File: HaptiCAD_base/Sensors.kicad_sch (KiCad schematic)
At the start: 6 parts, among them U501 AP2112K-3.3

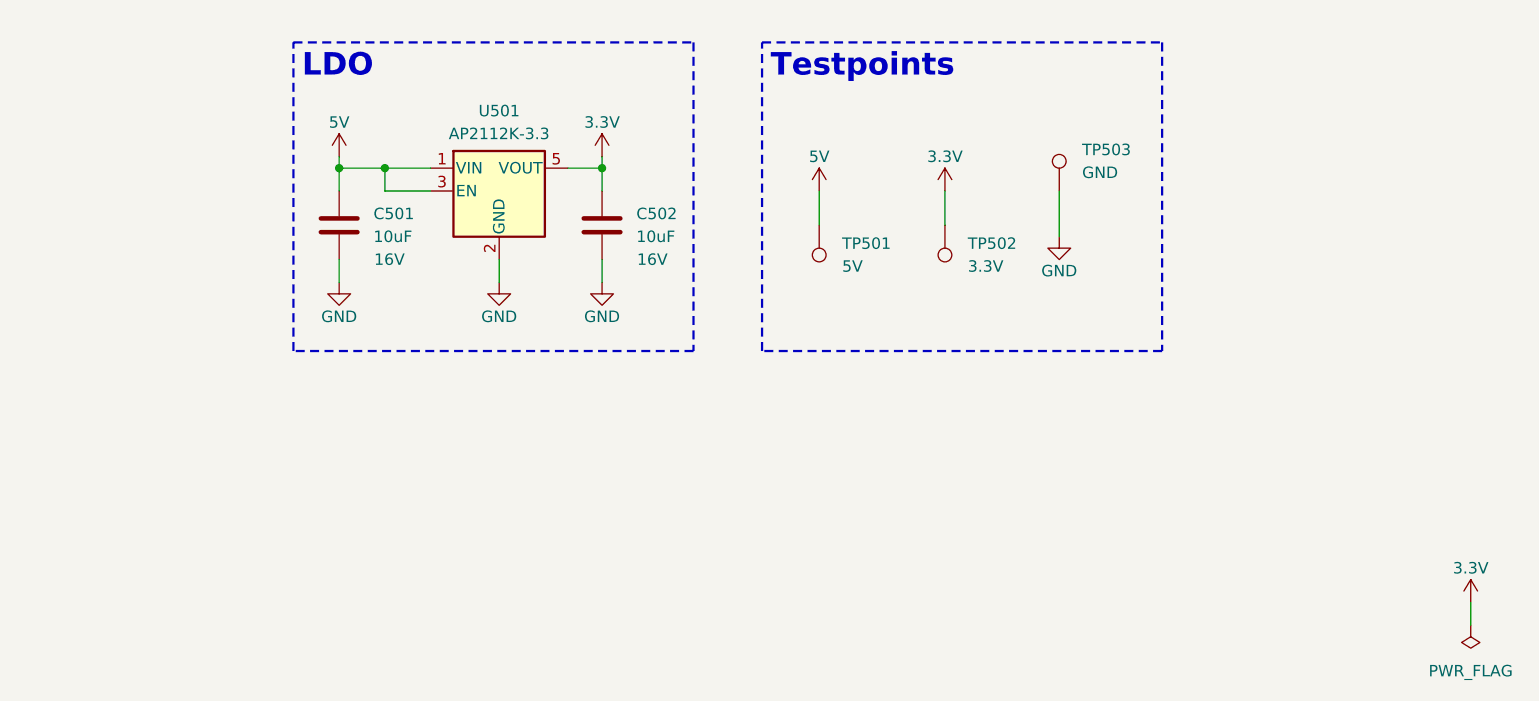
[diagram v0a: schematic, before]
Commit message: Split project into base and motor mount pcb
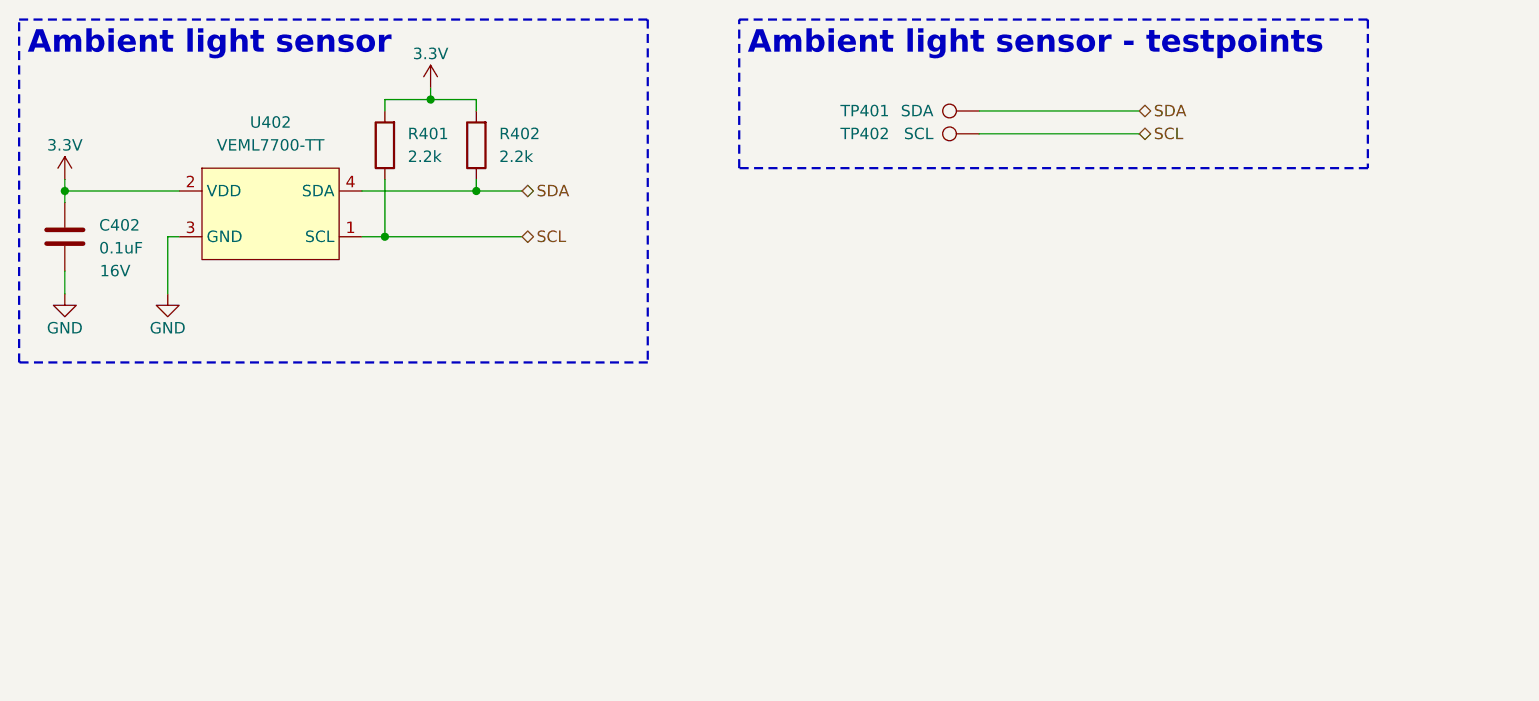
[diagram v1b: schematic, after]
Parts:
- removed C501, C502: 10uF, Capacitor_SMD:C_0805_2012Metric, symbol Device:C
- removed TP501: 5V, TestPoint:TestPoint_Pad_D1.0mm, symbol Connector:TestPoint
- removed TP502: 3.3V, TestPoint:TestPoint_Pad_D1.0mm, symbol Connector:TestPoint
- removed TP503: GND, TestPoint:TestPoint_Pad_D1.0mm, symbol Connector:TestPoint
- removed U501: AP2112K-3.3, Package_TO_SOT_SMD:SOT-23-5, symbol Regulator_Linear:AP2112K-3.3
- added C402: 0.1uF, Capacitor_SMD:C_0603_1608Metric, symbol Device:C
- added R401, R402: 2.2k, Resistor_SMD:R_0603_1608Metric, symbol Device:R
- added TP401: SDA, TestPoint:TestPoint_Pad_D1.0mm, symbol Connector:TestPoint
- added TP402: SCL, TestPoint:TestPoint_Pad_D1.0mm, symbol Connector:TestPoint
- added U402: VEML7700-TT, PCM_SparkFun-Sensor:VEML7700-TT, symbol PCM_SparkFun-Sensor:VEML7700-TT
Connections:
- net 3.3V: now also C402.1, R401.2, R402.2, U402.2 (VDD)
- net GND: now also C402.2, U402.3 (GND)
- new net SCL: R401.1, TP402.1, U402.1 (SCL)
- new net SDA: R402.1, TP401.1, U402.4 (SDA)
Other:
- title: Power -> Sensors

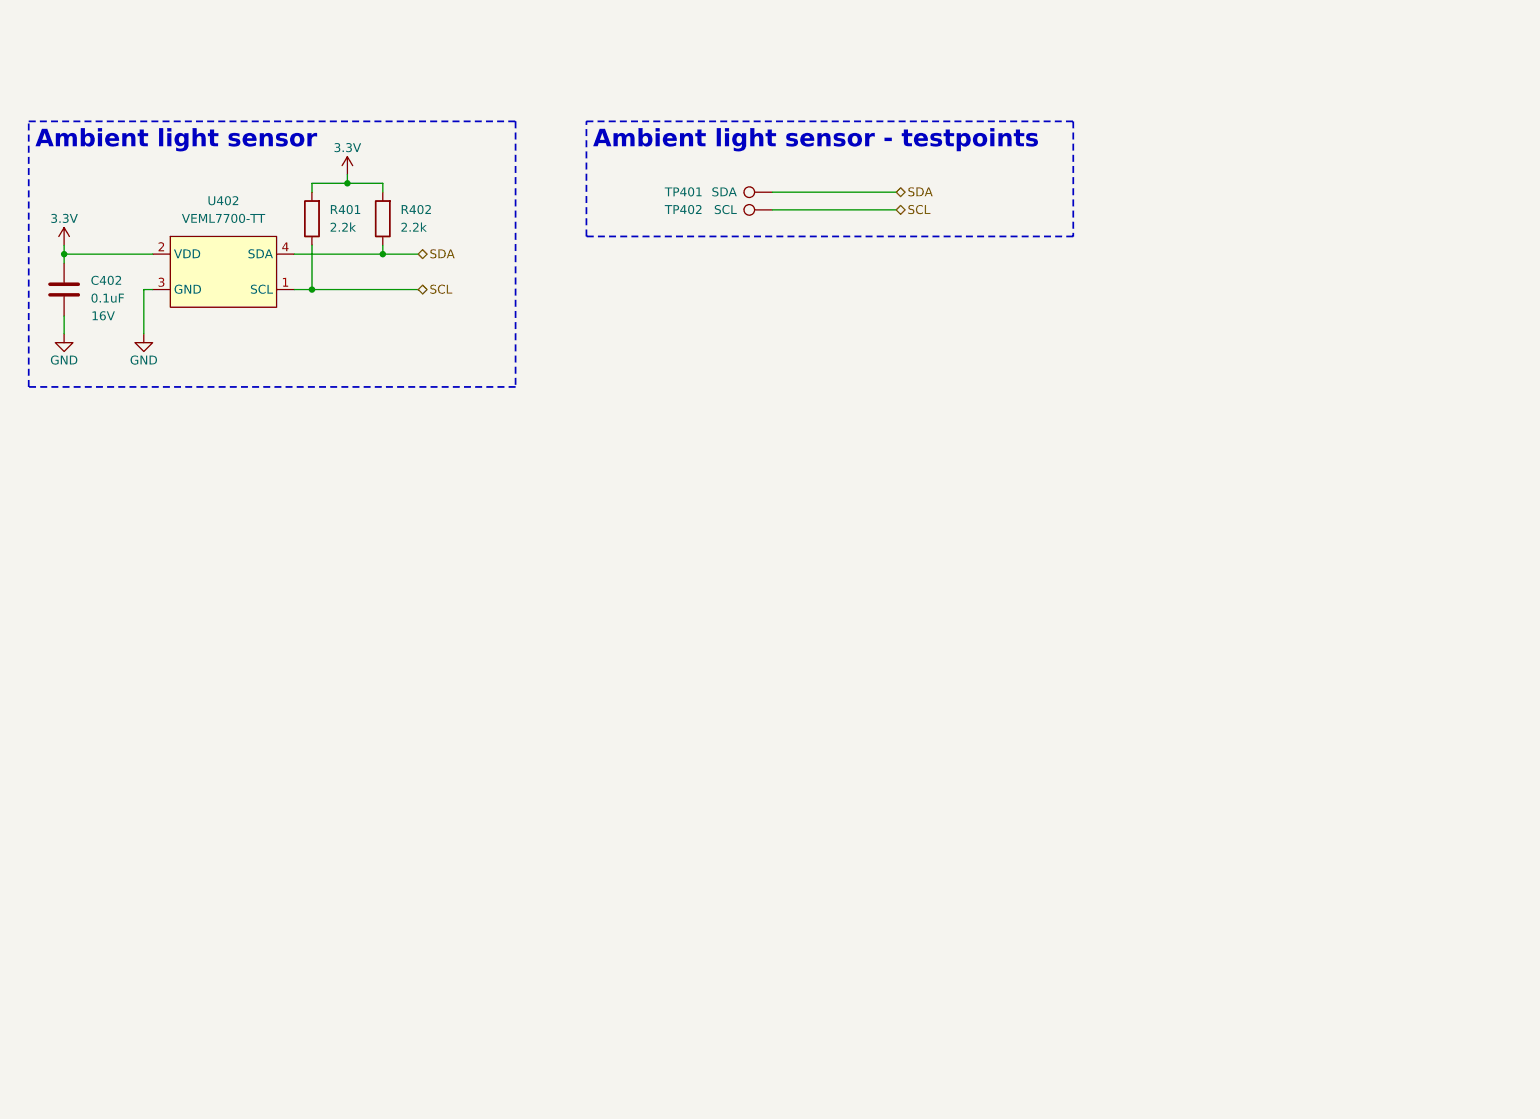
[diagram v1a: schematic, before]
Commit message: updated base schematic and PCB
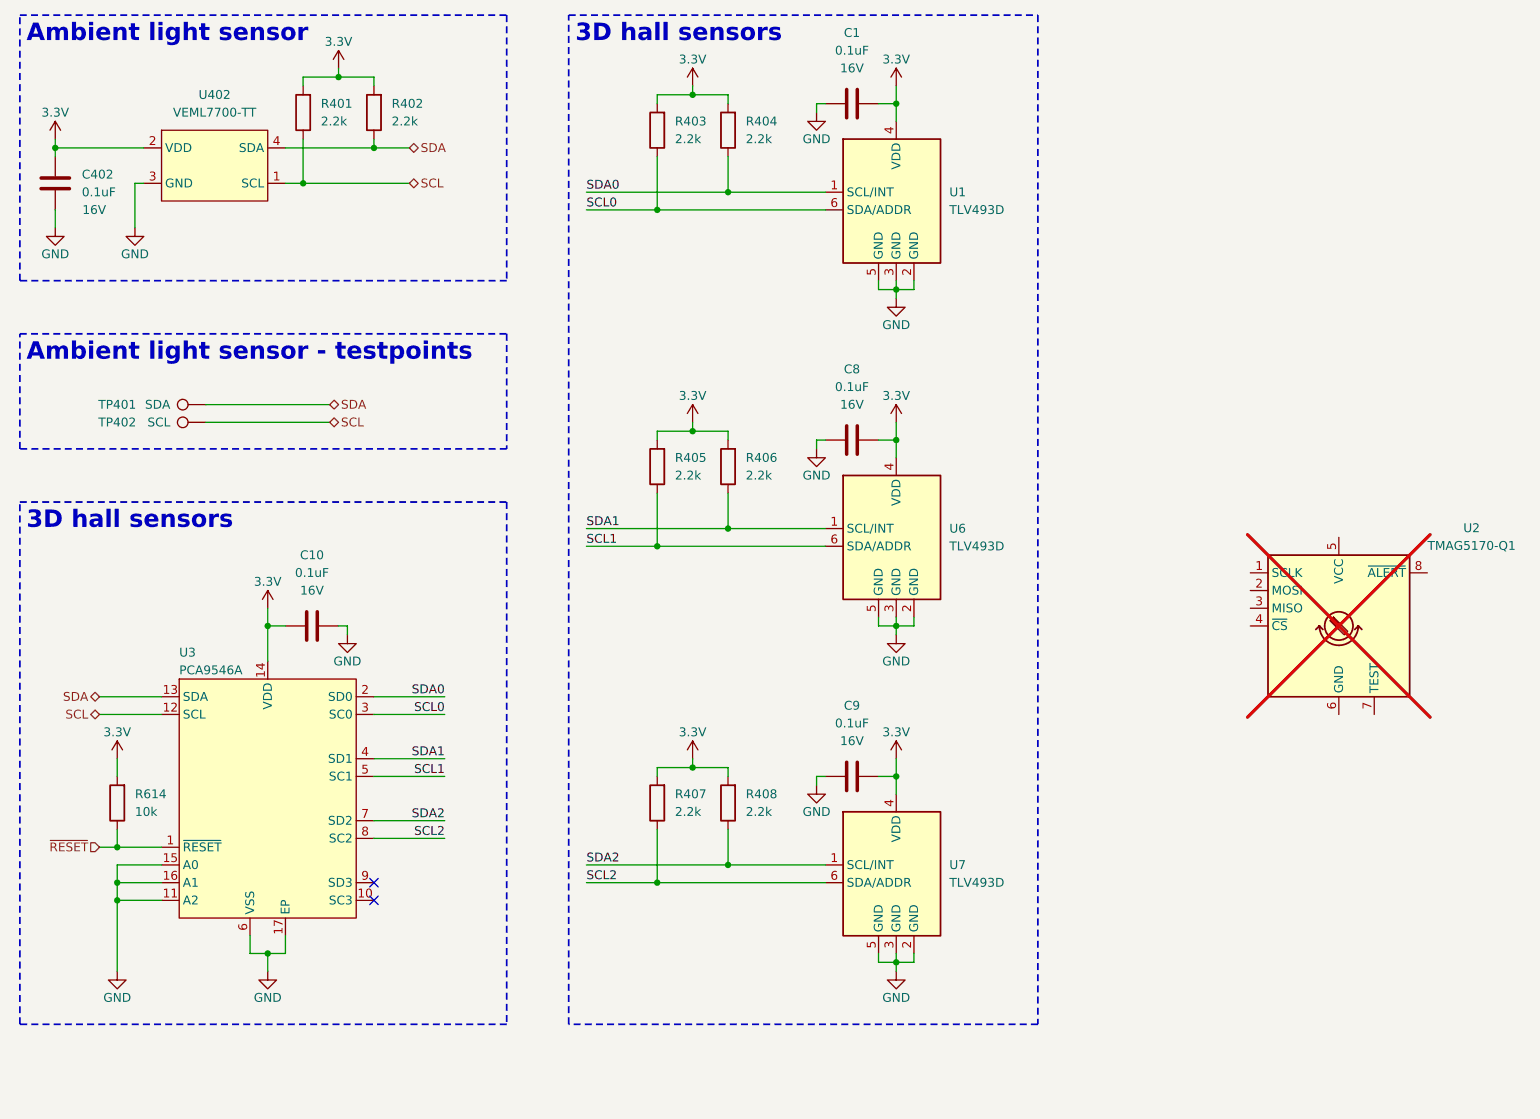
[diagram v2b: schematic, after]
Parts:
- added C1, C10, C8, C9: 0.1uF, Capacitor_SMD:C_0603_1608Metric, symbol Device:C
- added R403, R404, R405, R406, R407, R408: 2.2k, Resistor_SMD:R_0603_1608Metric, symbol Device:R
- added R614: 10k, Resistor_SMD:R_0402_1005Metric, symbol Device:R
- added U1, U6, U7: TLV493D, Package_TO_SOT_SMD:SOT-23-6, symbol Sensor_Magnetic:TLV493D
- added U2: TMAG5170-Q1, Package_SO:VSSOP-8_3x3mm_P0.65mm, symbol Sensor_Magnetic:TMAG5170-Q1
- added U3: PCA9546A, PCA9546A:QFN-16_EP_5.25x5.25_Pitch0.65mm, symbol PCA9546A:PCA9546A
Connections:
- net 3.3V: now also C1.2, C10.2, C8.2, C9.2, R403.2, R404.2, R405.2, R406.2, R407.2, R408.2, R614.2, U1.4 (VDD), U3.14 (VDD), U6.4 (VDD), U7.4 (VDD)
- net GND: now also C1.1, C10.1, C8.1, C9.1, U1.2 (GND), U1.3 (GND), U1.5 (GND), U3.11 (A2), U3.15 (A0), U3.16 (A1), U3.17 (EP), U3.6 (VSS), U6.2 (GND), U6.3 (GND), U6.5 (GND), U7.2 (GND), U7.3 (GND), U7.5 (GND)
- net SCL: now also U3.12 (SCL)
- net SDA: now also U3.13 (SDA)
- new net SCL0: R403.1, U1.6 (SDA/ADDR), U3.3 (SC0)
- new net SCL1: R405.1, U3.5 (SC1), U6.6 (SDA/ADDR)
- new net SCL2: R407.1, U3.8 (SC2), U7.6 (SDA/ADDR)
- new net SDA0: R404.1, U1.1 (SCL/INT), U3.2 (SD0)
- new net SDA1: R406.1, U3.4 (SD1), U6.1 (SCL/INT)
- new net SDA2: R408.1, U3.7 (SD2), U7.1 (SCL/INT)
- new net ~{RESET}: R614.1, U3.1 (~{RESET})
- no-connect marks 0 -> 2
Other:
- moved on the sheet: C402, R401, R402, TP401, TP402, U402

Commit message: Finished schematic of the base board
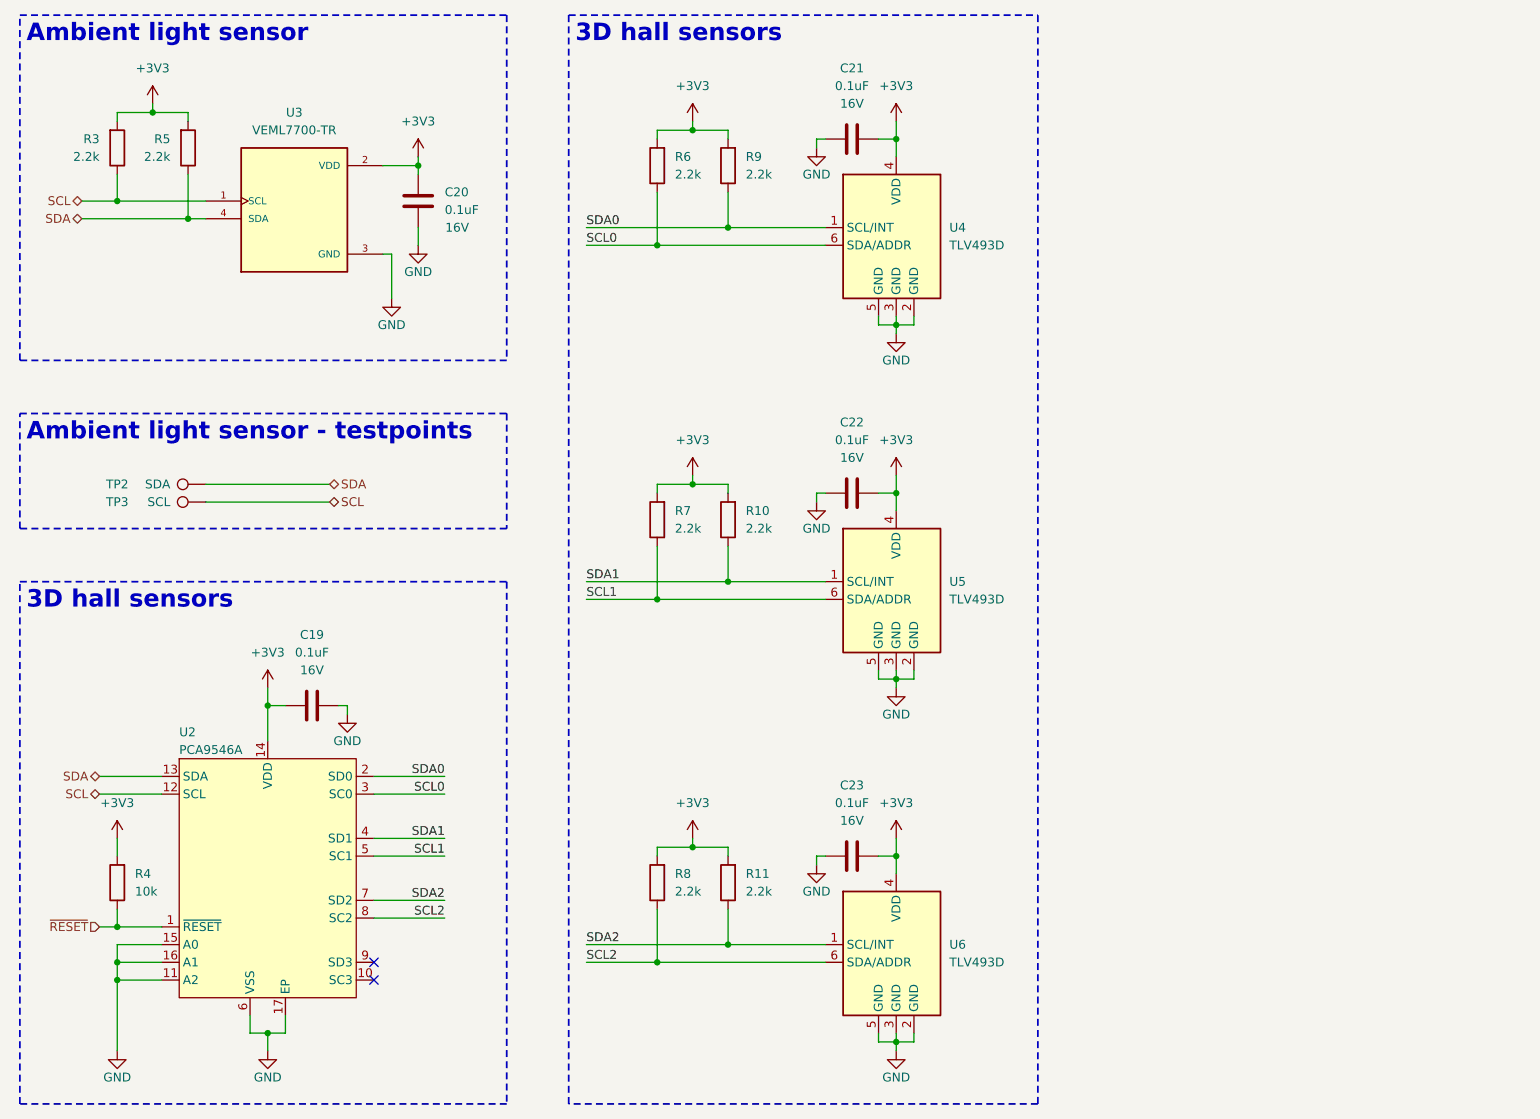
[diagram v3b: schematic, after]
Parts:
- removed U2: TMAG5170-Q1, Package_SO:VSSOP-8_3x3mm_P0.65mm, symbol Sensor_Magnetic:TMAG5170-Q1
- removed U402: VEML7700-TT, PCM_SparkFun-Sensor:VEML7700-TT, symbol PCM_SparkFun-Sensor:VEML7700-TT
- added U3: VEML7700-TR, VEML7700-TR:XDCR_VEML7700-TR, symbol VEML7700-TR:VEML7700-TR
- renumbered C10 to C19, C402 to C20, C1 to C21, C8 to C22, C9 to C23, R406 to R10, R408 to R11, R402 to R3, R614 to R4, R401 to R5, R403 to R6, R405 to R7, R407 to R8, R404 to R9, TP401 to TP2, TP402 to TP3, U3 to U2, U1 to U4, U6 to U5, U7 to U6
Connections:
- net GND: now also U3.3 (GND)
- net SCL: now also R3.1, U3.1 (SCL); no longer R5.1
- net SDA: now also R5.1, U3.4 (SDA); no longer R3.1
- net 3.3V renamed +3V3
- net +3V3: now also U3.2 (VDD)
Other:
- moved on the sheet: C19, C20, C21, C22, C23, R10, R11, R3, R4, R5, R6, R7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

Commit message: Finished the layout for the base and motor mount
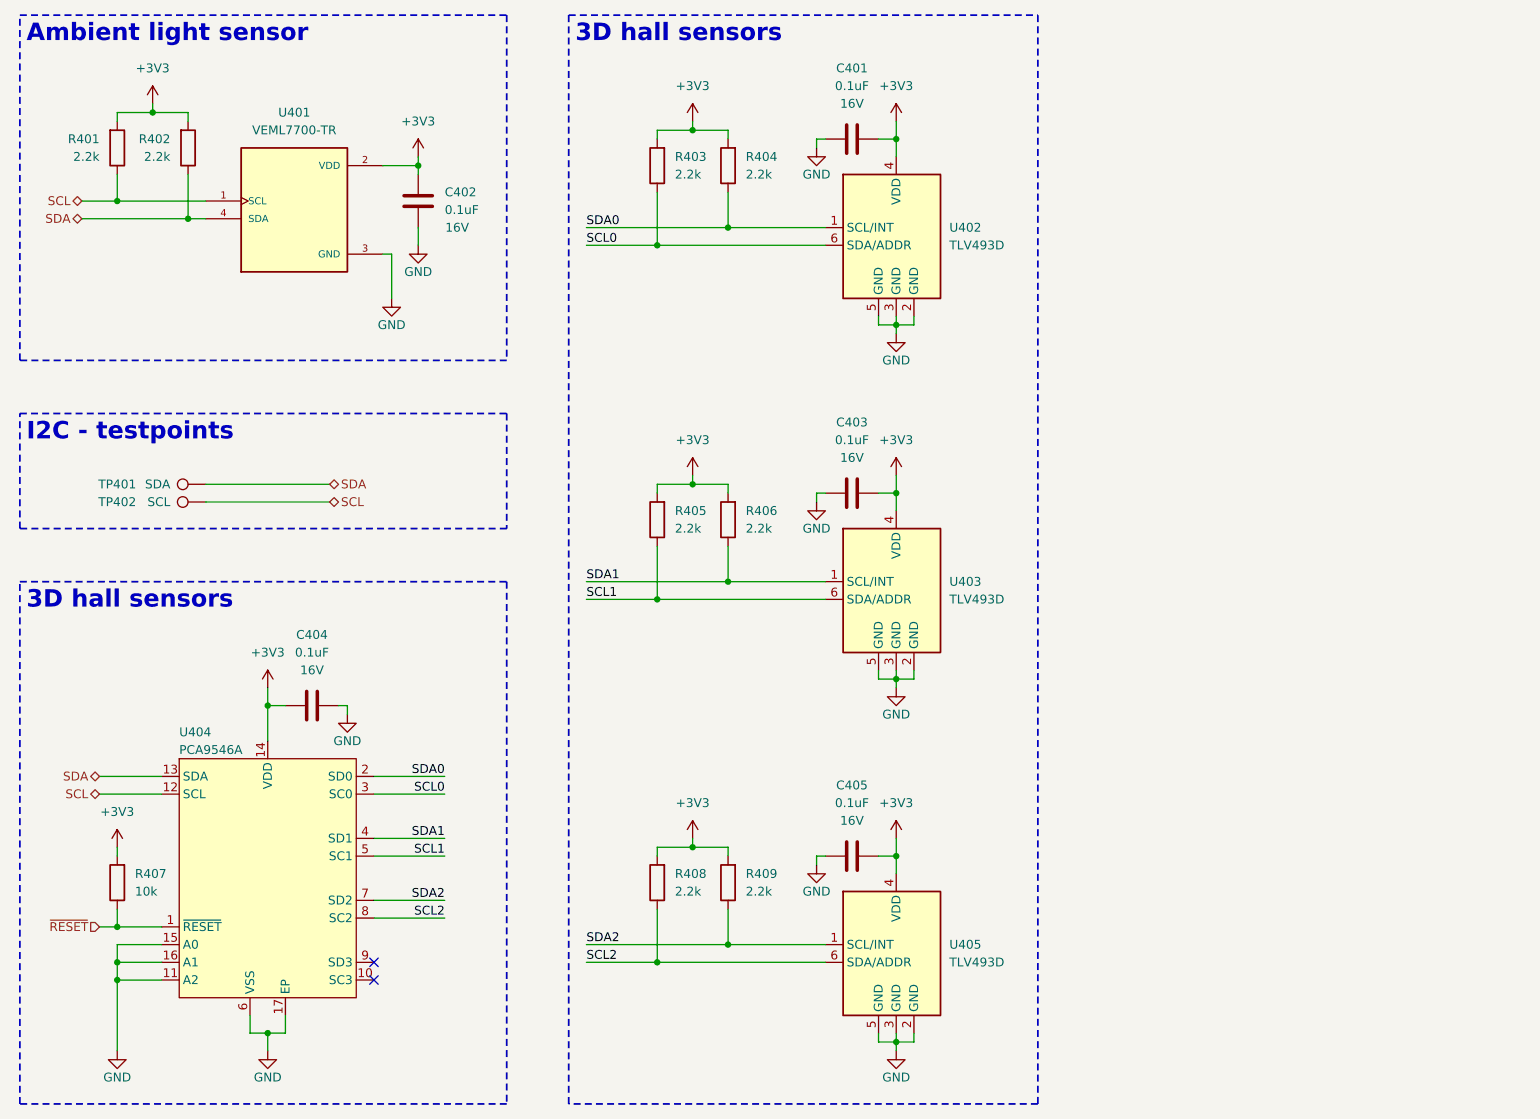
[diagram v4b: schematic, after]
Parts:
- renumbered C21 to C401, C20 to C402, C22 to C403, C19 to C404, C23 to C405, R3 to R401, R5 to R402, R6 to R403, R9 to R404, R7 to R405, R10 to R406, R4 to R407, R8 to R408, R11 to R409, TP2 to TP401, TP3 to TP402, U3 to U401, U4 to U402, U5 to U403, U2 to U404, U6 to U405
